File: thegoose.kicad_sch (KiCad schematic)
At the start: 62 parts, among them U1 DRV8848, U2 DRV8848, U3 DRV8848

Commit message: Finish initial schematic and assign footprints
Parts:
- C11, C7: value 100pF -> 100nF
- C12, C5, C8: footprint (none) -> Capacitor_SMD:C_1210_3225Metric_Pad1.42x2.65mm_HandSolder
- C15, C16: footprint (none) -> Capacitor_SMD:C_1206_3216Metric_Pad1.33x1.80mm_HandSolder
- L1: footprint (none) -> Inductor_SMD:L_1210_3225Metric_Pad1.42x2.65mm_HandSolder
- R25, R26, R27, R28: footprint (none) -> Resistor_SMD:R_1206_3216Metric_Pad1.30x1.75mm_HandSolder
- S1: value Motor_Servo -> IO_PORT_1; symbol Motor:Motor_Servo -> Connector_Generic:Conn_01x03
- S2: value Motor_Servo -> IO_PORT_2; symbol Motor:Motor_Servo -> Connector_Generic:Conn_01x03
- S3: value Motor_Servo -> IO_PORT_3; symbol Motor:Motor_Servo -> Connector_Generic:Conn_01x03
- S4: value Motor_Servo -> IO_PORT_4; symbol Motor:Motor_Servo -> Connector_Generic:Conn_01x03
- S5: value Motor_Servo -> IO_PORT_5; symbol Motor:Motor_Servo -> Connector_Generic:Conn_01x03
- S6: value Motor_Servo -> IO_PORT_6; symbol Motor:Motor_Servo -> Connector_Generic:Conn_01x03
- U4: value ~ -> AP64500SP-13; footprint (none) -> Package_SO:Diodes_SO-8EP
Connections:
- net +BATT: now also U4.2 (VIN), U4.3 (EN); no longer U4. (GND)
- net GND: now also U4.7 (GND), U4.9 (EP); no longer U4. (GND)
- net at C14.1, L1.1: now also U4.8 (SW); no longer U4. (GND)
- net at R25.2: now also U4.4 (RT/CLK); no longer U4. (GND)
- net at R26.1, R27.2: now also U4.5 (FB); no longer U4. (GND)
- net at R28.2: now also U4.6 (COMP); no longer U4. (GND)
- net at C14.2: now also U4.1 (BST); no longer U4. (GND)
- no-connect marks 10 -> 11

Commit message: Start on PCB
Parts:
- added BT1: XT30_SOLDER_CABLE, hexy:XT30_SolderPads_1x02_P5.00mm, symbol Connector_Generic:Conn_01x02
- C1, C10, C11, C13, C14, C15, C16, C2, C3, C4, C6, C7, C9: footprint Capacitor_SMD:C_1206_3216Metric_Pad1.33x1.80mm_HandSolder -> Capacitor_SMD:C_0805_2012Metric_Pad1.18x1.45mm_HandSolder
- C12, C5, C8: footprint Capacitor_SMD:C_1210_3225Metric_Pad1.42x2.65mm_HandSolder -> Capacitor_SMD:C_1206_3216Metric_Pad1.33x1.80mm_HandSolder
- R1, R10, R11, R12, R13, R14, R15, R16, R17, R18, R19, R2, R20, R21, R22, R23, R24, R25, R26, R27, R28, R3, R4, R5, R6, R7, R8, R9: footprint Resistor_SMD:R_1206_3216Metric_Pad1.30x1.75mm_HandSolder -> Resistor_SMD:R_0805_2012Metric_Pad1.20x1.40mm_HandSolder
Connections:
- net +BATT: now also BT1.1 (Pin_1)
- net GND: now also BT1.2 (Pin_2)
- net at ESP32.16 (D23), R22.2, U3.16 (AIN1): no longer R21.2
- net at ESP32.17 (D22), U3.15 (AIN2): now also R21.2
- net at ESP32.3 (D13), R14.2, U1.16 (AIN1): no longer R13.2
- net at ESP32.4 (D12), U1.15 (AIN2): now also R13.2
- net at ESP32.7 (D26), R18.2, U2.16 (AIN1): no longer R17.2
- net at ESP32.8 (D25), U2.15 (AIN2): now also R17.2

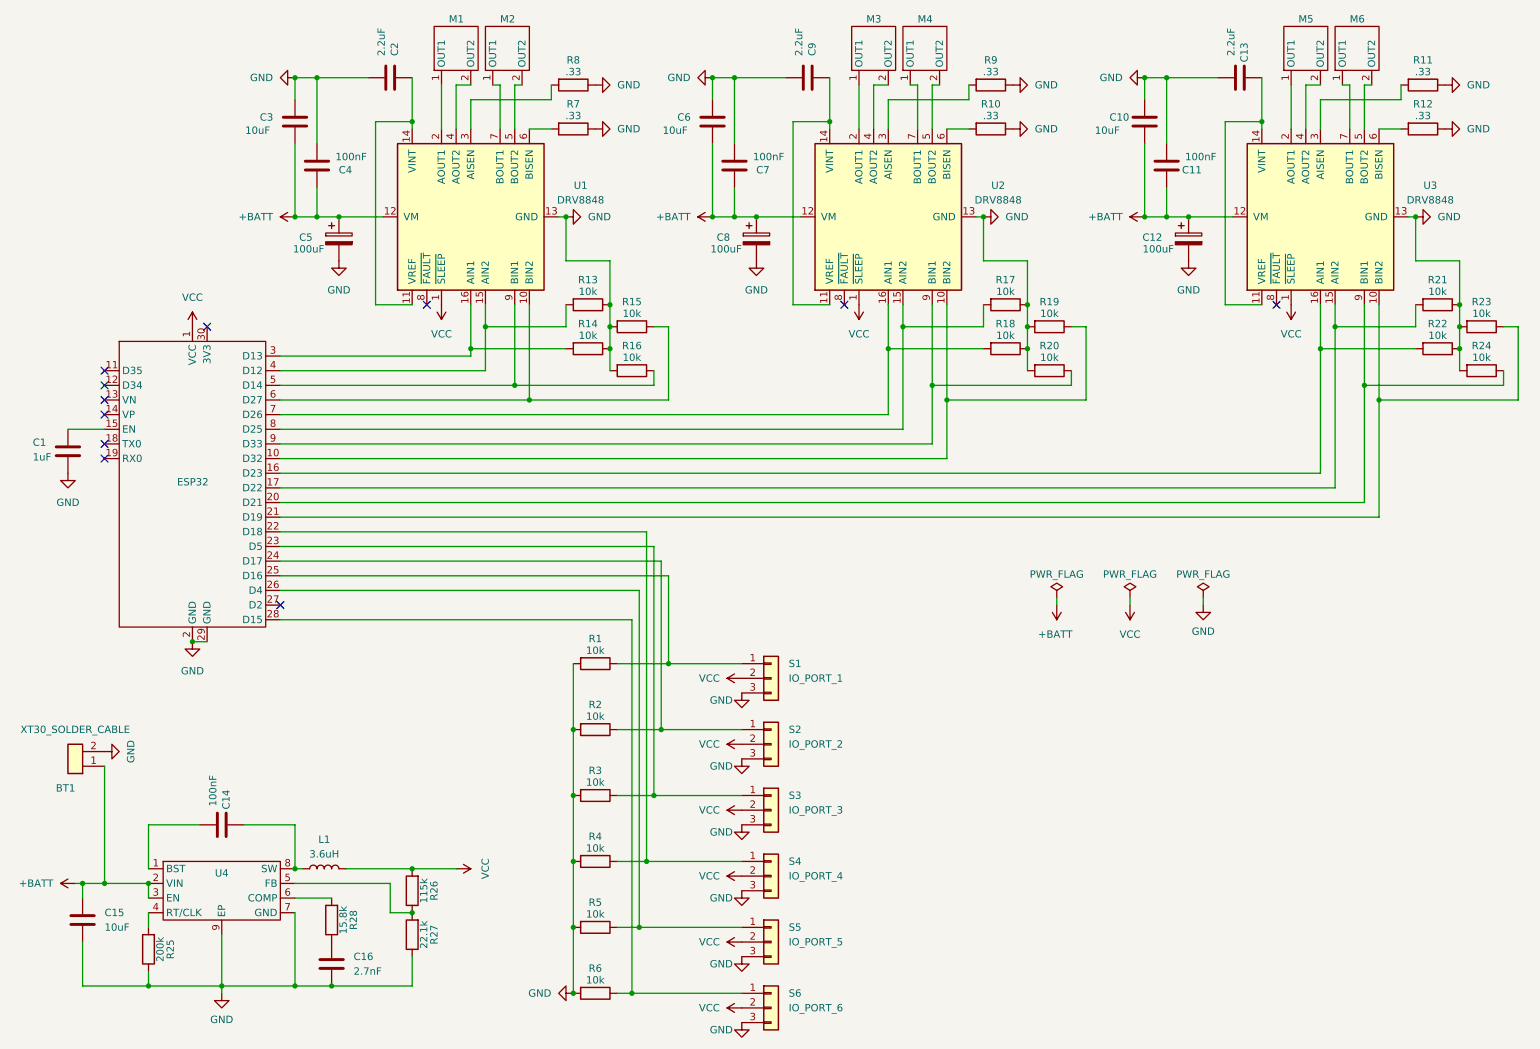
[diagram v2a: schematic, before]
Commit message: Clean up schematic layout
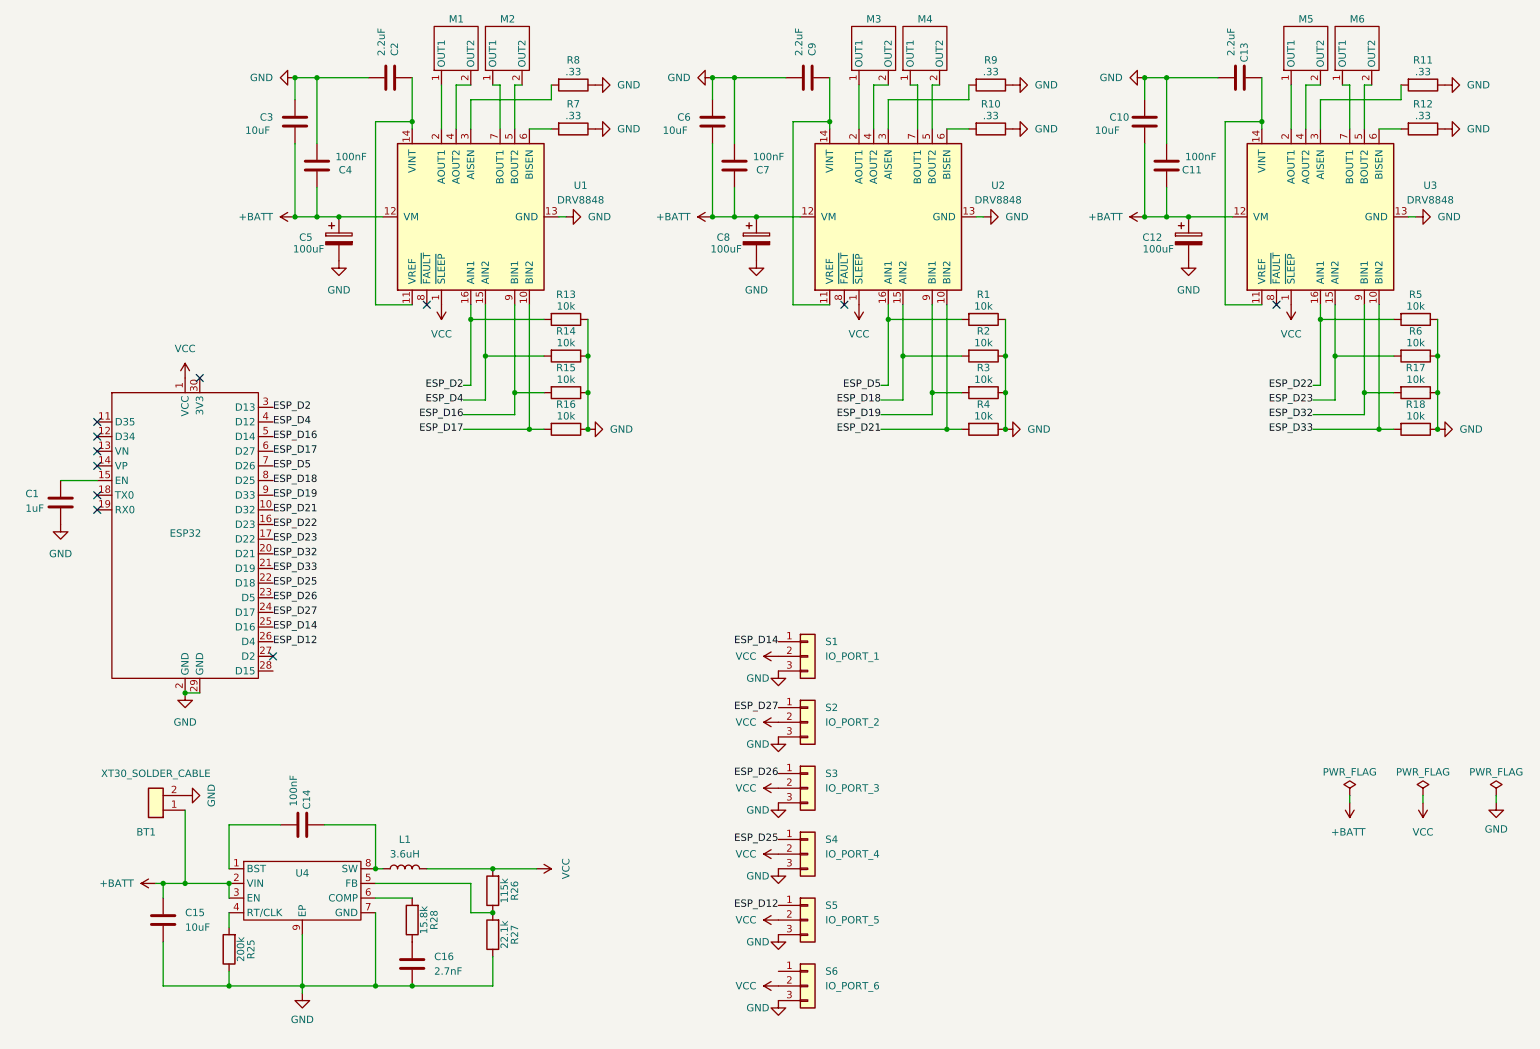
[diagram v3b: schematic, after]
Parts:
- removed R19, R20, R21, R22, R23, R24: 10k, Resistor_SMD:R_0805_2012Metric_Pad1.20x1.40mm_HandSolder, symbol Device:R
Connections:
- net GND: now also R1.1, R15.1, R16.1, R2.1, R3.1, R4.1, R5.1, R6.1; no longer R1.2, R15.2, R16.2, R2.2, R3.2, R4.2, R5.2, R6.2
- net ESP_D21: now reaches ESP32.10 (D32), U2.10 (BIN2)
- net ESP_D21: now also R4.2
- net ESP_D22: now reaches ESP32.16 (D23), U3.16 (AIN1)
- net ESP_D22: now also R5.2
- net ESP_D23: now reaches ESP32.17 (D22), U3.15 (AIN2)
- net ESP_D23: now also R6.2
- net ESP_D32: now reaches ESP32.20 (D21), U3.9 (BIN1)
- net ESP_D32: now also R17.2
- net ESP_D33: now reaches ESP32.21 (D19), U3.10 (BIN2)
- net ESP_D33: now also R18.2
- net ESP_D25: now reaches ESP32.22 (D18), S4.1 (Pin_1)
- net ESP_D25: no longer R4.1
- net ESP_D26: now reaches ESP32.23 (D5), S3.1 (Pin_1)
- net ESP_D26: no longer R3.1
- net ESP_D27: now reaches ESP32.24 (D17), S2.1 (Pin_1)
- net ESP_D27: no longer R2.1
- net ESP_D14: now reaches ESP32.25 (D16), S1.1 (Pin_1)
- net ESP_D14: no longer R1.1
- net ESP_D12: now reaches ESP32.26 (D4), S5.1 (Pin_1)
- net ESP_D12: no longer R5.1
- net ESP_D2: now reaches ESP32.3 (D13), U1.16 (AIN1)
- net ESP_D2: now also R13.2; no longer R14.2
- net ESP_D4: now reaches ESP32.4 (D12), U1.15 (AIN2)
- net ESP_D4: now also R14.2; no longer R13.2
- net ESP_D16: now reaches ESP32.5 (D14), U1.9 (BIN1)
- net ESP_D16: now also R15.2; no longer R16.1
- net ESP_D17: now reaches ESP32.6 (D27), U1.10 (BIN2)
- net ESP_D17: now also R16.2; no longer R15.1
- net ESP_D5: now reaches ESP32.7 (D26), U2.16 (AIN1)
- net ESP_D5: now also R1.2; no longer R18.2
- net ESP_D18: now reaches ESP32.8 (D25), U2.15 (AIN2)
- net ESP_D18: now also R2.2; no longer R17.2
- net ESP_D19: now reaches ESP32.9 (D33), U2.9 (BIN1)
- net ESP_D19: now also R3.2
- now unconnected: ESP32.28 (D15), S6.1 (Pin_1)
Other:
- moved on the sheet: BT1, C1, C14, C15, C16, L1, R13, R14, R15, R16, R25, R26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

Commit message: Fix missing net
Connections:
- net ESP_D15: now reaches ESP32.28 (D15)
- net ESP_D15: now also S6.1 (Pin_1)
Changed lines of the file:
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@@
+		)
+	)
+	(label "ESP_D15"
+		(at 59.69 129.54 0)
+		(effects
+			(font
+				(size 1.27 1.27)
+			)
+			(justify left bottom)
+		)
+	)
+	(label "ESP_D15"
+		(at 147.32 181.61 180)
+		(effects
+			(font
+				(size 1.27 1.27)
+			)
+			(justify right bottom)
 		)
 	)

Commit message: Relabel everything
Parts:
- removed R1, R13, R14, R15, R16, R17, R18, R2, R3, R4, R5, R6: 10k, Resistor_SMD:R_0805_2012Metric_Pad1.20x1.40mm_HandSolder, symbol Device:R
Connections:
- net ESP_D12: now also ESP32.4 (D12), U1.9 (BIN1); no longer ESP32.26 (D4), S5.1 (Pin_1)
- net ESP_D14: now also ESP32.5 (D14), U1.15 (AIN2); no longer ESP32.25 (D16), S1.1 (Pin_1)
- net ESP_D16: now also ESP32.25 (D16), S2.1 (Pin_1); no longer ESP32.5 (D14), U1.9 (BIN1)
- net ESP_D17: now also ESP32.24 (D17), S3.1 (Pin_1); no longer ESP32.6 (D27), U1.10 (BIN2)
- net ESP_D18: now also ESP32.22 (D18), S5.1 (Pin_1); no longer ESP32.8 (D25), U2.15 (AIN2)
- net ESP_D19: now also ESP32.21 (D19), U3.16 (AIN1); no longer ESP32.9 (D33), U2.9 (BIN1)
- net ESP_D2: now also ESP32.27 (D2), U1.1 (~{SLEEP}), U2.1 (~{SLEEP}), U3.1 (~{SLEEP}); no longer ESP32.3 (D13), U1.16 (AIN1)
- net ESP_D21: now also ESP32.20 (D21), U3.15 (AIN2); no longer ESP32.10 (D32), U2.10 (BIN2)
- net ESP_D22: now also ESP32.17 (D22), U3.9 (BIN1); no longer ESP32.16 (D23), U3.16 (AIN1)
- net ESP_D23: now also ESP32.16 (D23), U3.10 (BIN2); no longer ESP32.17 (D22), U3.15 (AIN2)
- net ESP_D25: now also ESP32.8 (D25), U2.9 (BIN1); no longer ESP32.22 (D18), S4.1 (Pin_1)
- net ESP_D26: now also ESP32.7 (D26), U2.10 (BIN2); no longer ESP32.23 (D5), S3.1 (Pin_1)
- net ESP_D27: now also ESP32.6 (D27), U1.16 (AIN1); no longer ESP32.24 (D17), S2.1 (Pin_1)
- net ESP_D32: now also ESP32.10 (D32), U2.16 (AIN1); no longer ESP32.20 (D21), U3.9 (BIN1)
- net ESP_D33: now also ESP32.9 (D33), U2.15 (AIN2); no longer ESP32.21 (D19), U3.10 (BIN2)
- net ESP_D4: now also ESP32.26 (D4), S1.1 (Pin_1); no longer ESP32.4 (D12), U1.15 (AIN2)
- net ESP_D5: now also ESP32.23 (D5), S4.1 (Pin_1); no longer ESP32.7 (D26), U2.16 (AIN1)
- net VCC: no longer U1.1 (~{SLEEP}), U2.1 (~{SLEEP}), U3.1 (~{SLEEP})
- new net ESP_D13: ESP32.3 (D13), U1.10 (BIN2)
- no-connect marks 11 -> 10
